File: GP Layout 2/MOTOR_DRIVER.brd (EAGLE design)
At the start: 91.4 x 97.5 mm, 82 parts, among them T1 2N2222, T2 2N2222, U7 ATMEGA328P_TQFP, Y1 16MHz

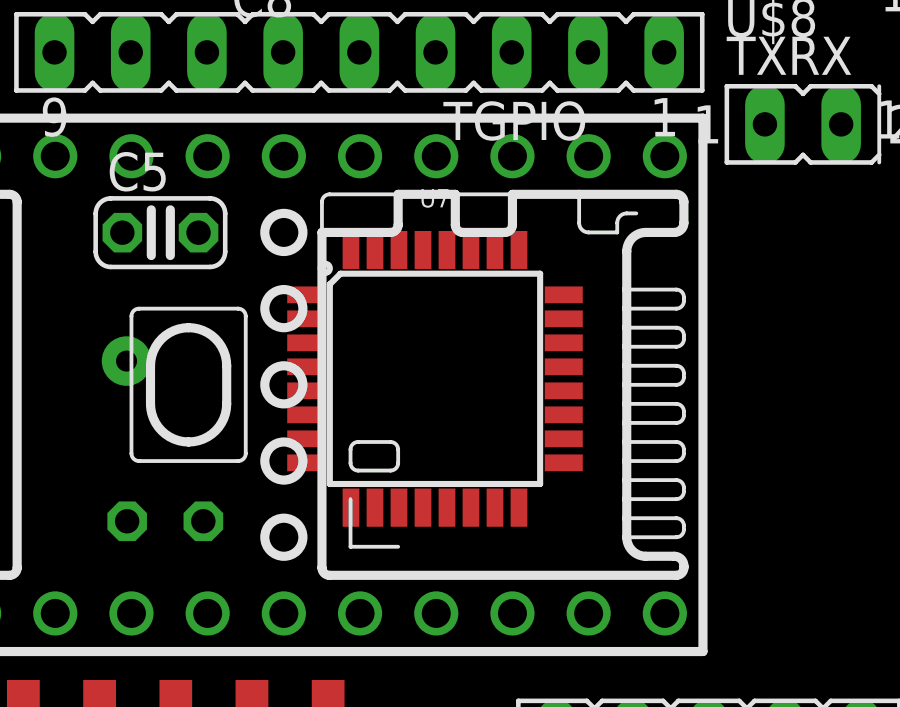
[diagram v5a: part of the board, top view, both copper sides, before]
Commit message: batt voltage connection fixed
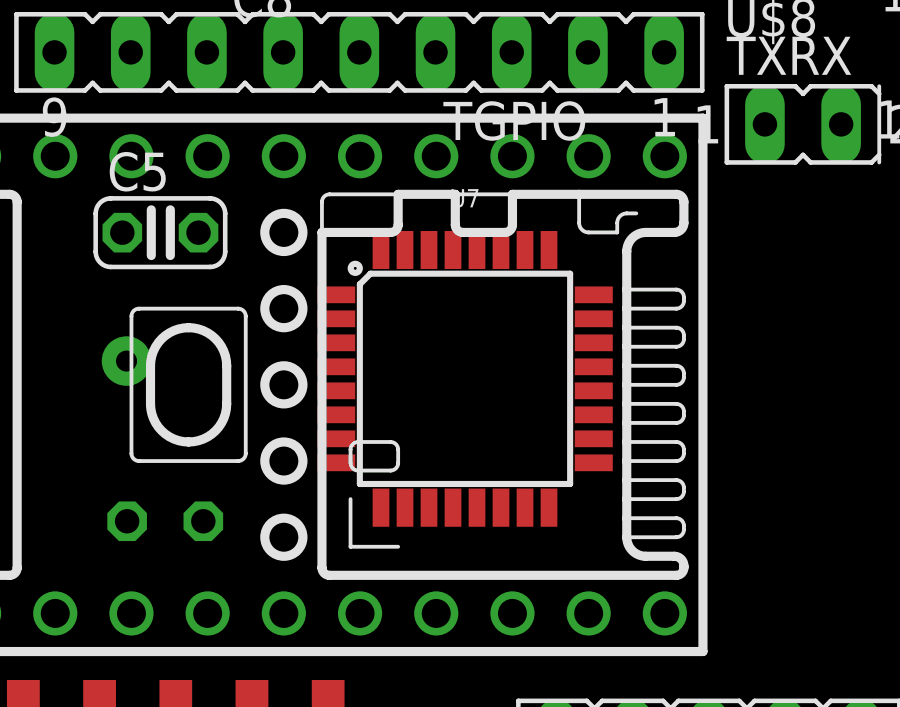
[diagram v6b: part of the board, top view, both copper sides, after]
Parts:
- moved U7 1.00 mm to (55.9, 21.5)
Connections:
- net 7_4V: now also R1.2
- net BATT_VOLTAGE: no longer R1.2
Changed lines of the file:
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@@
 <attribute name="VENDOR" value="Microchip" x="34.88" y="74.33" size="1.778" layer="28" rot="MR270" display="off"/>
 </element>
-<element name="U7" library="SparkFun-IC-Microcontroller" package="TQFP32-08" value="ATMEGA328P_TQFP" x="54.922" y="21.518">
-<attribute name="PROD_ID" value="IC-09069" x="54.922" y="21.518" size="1.778" layer="27" display="off"/>
+<element name="U7" library="SparkFun-IC-Microcontroller" package="TQFP32-08" value="ATMEGA328P_TQFP" x="55.922" y="21.518">
+<attribute name="PROD_ID" value="IC-09069" x="55.922" y="21.518" size="1.778" layer="27" display="off"/>
 </element>
 <element name="Y1" library="SparkFun-Clocks" package="HC49US" value="16MHz" x="42.1" y="22.11" rot="MR0">
@@
 <wire x1="74.626" y1="30.162" x2="74.826" y2="34.402" width="0" layer="19" extent="1-1"/>
 <wire x1="74.55" y1="41.066" x2="74.826" y2="34.402" width="0" layer="19" extent="1-1"/>
-<wire x1="59.2146" y1="21.918" x2="74.626" y2="30.162" width="0" layer="19" extent="1-1"/>
-<wire x1="50.6294" y1="21.118" x2="59.2146" y2="21.918" width="0" layer="19" extent="1-1"/>
-<wire x1="50.6294" y1="22.718" x2="50.6294" y2="21.118" width="0" layer="19" extent="1-1"/>
-<wire x1="47.04" y1="26.39" x2="50.6294" y2="22.718" width="0" layer="19" extent="1-1"/>
-<wire x1="47.2" y1="16.77" x2="50.6294" y2="21.118" width="0" layer="19" extent="1-1"/>
+<wire x1="60.2146" y1="21.918" x2="74.626" y2="30.162" width="0" layer="19" extent="1-1"/>
+<wire x1="51.6294" y1="21.118" x2="60.2146" y2="21.918" width="0" layer="19" extent="1-1"/>
+<wire x1="51.6294" y1="22.718" x2="51.6294" y2="21.118" width="0" layer="19" extent="1-1"/>
+<wire x1="47.04" y1="26.39" x2="51.6294" y2="22.718" width="0" layer="19" extent="1-1"/>
+<wire x1="47.2" y1="16.77" x2="51.6294" y2="21.118" width="0" layer="19" extent="1-1"/>
 <wire x1="46.28" y1="10.4758" x2="47.2" y2="16.77" width="0" layer="19" extent="1-1"/>
 <wire x1="43.74" y1="10.4758" x2="46.28" y2="10.4758" width="0" layer="19" extent="1-1"/>
@@
 <wire x1="24.414" y1="33.51" x2="33.02" y2="40.64" width="0" layer="19" extent="1-1"/>
 <wire x1="25.302" y1="22.49" x2="24.414" y2="33.51" width="0" layer="19" extent="1-1"/>
-<wire x1="69.13" y1="9.514" x2="59.2146" y2="21.918" width="0" layer="19" extent="1-1"/>
+<wire x1="69.13" y1="9.514" x2="60.2146" y2="21.918" width="0" layer="19" extent="1-1"/>
 <wire x1="75.142" y1="9.45" x2="69.13" y2="9.514" width="0" layer="19" extent="1-1"/>
 <wire x1="89" y1="10.54" x2="75.142" y2="9.45" width="0" layer="19" extent="1-1"/>
@@
 <contactref element="C6" pad="1"/>
 <contactref element="Y1" pad="1"/>
-<wire x1="44.64" y1="22.11" x2="50.6294" y2="19.518" width="0" layer="19" extent="1-1"/>
+<wire x1="44.64" y1="22.11" x2="51.6294" y2="19.518" width="0" layer="19" extent="1-1"/>
 <wire x1="44.66" y1="16.77" x2="44.64" y2="22.11" width="0" layer="19" extent="1-1"/>
 </signal>
@@
 <contactref element="U7" pad="8"/>
 <wire x1="39.56" y1="22.11" x2="44.5" y2="26.39" width="0" layer="19" extent="1-1"/>
-<wire x1="50.6294" y1="18.718" x2="39.56" y2="22.11" width="0" layer="19" extent="1-1"/>
+<wire x1="51.6294" y1="18.718" x2="39.56" y2="22.11" width="0" layer="19" extent="1-1"/>
 </signal>
 <signal name="SPI_MOSI">
@@
 <contactref element="U7" pad="15"/>
 <contactref element="PROGRAM" pad="4"/>
-<wire x1="37.184" y1="13.698" x2="56.922" y2="17.2254" width="0" layer="19" extent="1-1"/>
+<wire x1="37.184" y1="13.698" x2="57.922" y2="17.2254" width="0" layer="19" extent="1-1"/>
 <wire x1="85.54" y1="23.26" x2="37.184" y2="13.698" width="0" layer="19" extent="1-1"/>
 </signal>
@@
 <contactref element="U$1" pad="13/SCK"/>
 <contactref element="PROGRAM" pad="3"/>
-<wire x1="37.184" y1="28.938" x2="59.2146" y2="18.718" width="0" layer="19" extent="1-1"/>
+<wire x1="37.184" y1="28.938" x2="60.2146" y2="18.718" width="0" layer="19" extent="1-1"/>
 <wire x1="83" y1="23.26" x2="37.184" y2="28.938" width="0" layer="19" extent="1-1"/>
 </signal>
@@
 <contactref element="U$1" pad="11/MOSI"/>
 <contactref element="PROGRAM" pad="1"/>
-<wire x1="34.644" y1="13.698" x2="57.722" y2="17.2254" width="0" layer="19" extent="1-1"/>
+<wire x1="34.644" y1="13.698" x2="58.722" y2="17.2254" width="0" layer="19" extent="1-1"/>
 <wire x1="83" y1="25.8" x2="34.644" y2="13.698" width="0" layer="19" extent="1-1"/>
 </signal>
@@
 <contactref element="U7" pad="11"/>
 <contactref element="CAMERA" pad="5"/>
-<wire x1="53.722" y1="17.2254" x2="85.302" y2="9.45" width="0" layer="19" extent="1-1"/>
+<wire x1="54.722" y1="17.2254" x2="85.302" y2="9.45" width="0" layer="19" extent="1-1"/>
 </signal>
 <signal name="CAMERA_A0">
 <contactref element="U7" pad="23"/>
 <contactref element="CAMERA" pad="3"/>
-<wire x1="59.2146" y1="23.518" x2="80.222" y2="9.45" width="0" layer="19" extent="1-1"/>
+<wire x1="60.2146" y1="23.518" x2="80.222" y2="9.45" width="0" layer="19" extent="1-1"/>
 </signal>
 <signal name="SERVO">
@@
 <contactref element="U7" pad="14"/>
 <contactref element="U$1" pad="10/CS"/>
-<wire x1="32.104" y1="13.698" x2="56.122" y2="17.2254" width="0" layer="19" extent="1-1"/>
+<wire x1="32.104" y1="13.698" x2="57.122" y2="17.2254" width="0" layer="19" extent="1-1"/>
 </signal>
 <signal name="RX">
 <contactref element="U7" pad="30"/>
 <contactref element="TXRX" pad="1"/>
-<wire x1="65.92" y1="30" x2="53.722" y2="25.8106" width="0" layer="19" extent="1-1"/>
+<wire x1="65.92" y1="30" x2="54.722" y2="25.8106" width="0" layer="19" extent="1-1"/>
 </signal>
 <signal name="TX">
 <contactref element="U7" pad="31"/>
 <contactref element="TXRX" pad="2"/>
-<wire x1="68.46" y1="30" x2="52.922" y2="25.8106" width="0" layer="19" extent="1-1"/>
+<wire x1="68.46" y1="30" x2="53.922" y2="25.8106" width="0" layer="19" extent="1-1"/>
 </signal>
 <signal name="5V">
@@
 <contactref element="U7" pad="18"/>
 <contactref element="U7" pad="29"/>
-<wire x1="59.2146" y1="19.518" x2="51.36" y2="1.4842" width="0" layer="19" extent="1-1"/>
-<wire x1="54.522" y1="25.8106" x2="59.2146" y2="19.518" width="0" layer="19" extent="1-1"/>
-<wire x1="50.6294" y1="21.918" x2="54.522" y2="25.8106" width="0" layer="19" extent="1-1"/>
-<wire x1="50.6294" y1="20.318" x2="50.6294" y2="21.918" width="0" layer="19" extent="1-1"/>
-<wire x1="4.164" y1="28.938" x2="50.6294" y2="21.918" width="0" layer="19" extent="1-1"/>
+<wire x1="60.2146" y1="19.518" x2="51.36" y2="1.4842" width="0" layer="19" extent="1-1"/>
+<wire x1="55.522" y1="25.8106" x2="60.2146" y2="19.518" width="0" layer="19" extent="1-1"/>
+<wire x1="51.6294" y1="21.918" x2="55.522" y2="25.8106" width="0" layer="19" extent="1-1"/>
+<wire x1="51.6294" y1="20.318" x2="51.6294" y2="21.918" width="0" layer="19" extent="1-1"/>
+<wire x1="4.164" y1="28.938" x2="51.6294" y2="21.918" width="0" layer="19" extent="1-1"/>
 </signal>
 <signal name="GND_TOP">
@@
 <contactref element="VOLT_REG" pad="3"/>
 <contactref element="SV1" pad="7"/>
+<contactref element="R1" pad="2"/>
 <wire x1="25.4" y1="40.64" x2="48.766" y2="40.246" width="0" layer="19" extent="1-1"/>
+<wire x1="32.058" y1="22.49" x2="25.4" y2="40.64" width="0" layer="19" extent="1-1"/>
 </signal>
 <signal name="BATT_VOLTAGE">
@@
 <contactref element="FUSE" pad="C"/>
 <contactref element="FUSE" pad="A"/>
-<contactref element="R1" pad="2"/>
-<wire x1="14.888" y1="75.846" x2="32.058" y2="22.49" width="0" layer="19" extent="1-1"/>
+<wire x1="14.888" y1="75.846" x2="6.27" y2="83.01" width="0" layer="19" extent="1-1"/>
 <wire x1="14.888" y1="69.786" x2="14.888" y2="75.846" width="0" layer="19" extent="1-1"/>
-<wire x1="6.27" y1="83.01" x2="14.888" y2="69.786" width="0" layer="19" extent="1-1"/>
 </signal>
 <signal name="N$21">
@@
 <contactref element="U7" pad="32"/>
 <contactref element="HALL1" pad="3"/>
-<wire x1="52.122" y1="25.8106" x2="77.366" y2="34.402" width="0" layer="19" extent="1-1"/>
+<wire x1="53.122" y1="25.8106" x2="77.366" y2="34.402" width="0" layer="19" extent="1-1"/>
 </signal>
 <signal name="CAMERA_CL">
 <contactref element="CAMERA" pad="4"/>
 <contactref element="U7" pad="12"/>
-<wire x1="54.522" y1="17.2254" x2="82.762" y2="9.45" width="0" layer="19" extent="1-1"/>
+<wire x1="55.522" y1="17.2254" x2="82.762" y2="9.45" width="0" layer="19" extent="1-1"/>
 </signal>
 <signal name="CAMERA_SI_B">
@@
 <contactref element="HALL2" pad="3"/>
 <contactref element="U7" pad="1"/>
-<wire x1="50.6294" y1="24.318" x2="77.166" y2="30.162" width="0" layer="19" extent="1-1"/>
+<wire x1="51.6294" y1="24.318" x2="77.166" y2="30.162" width="0" layer="19" extent="1-1"/>
 </signal>
 <signal name="HALL1_B">

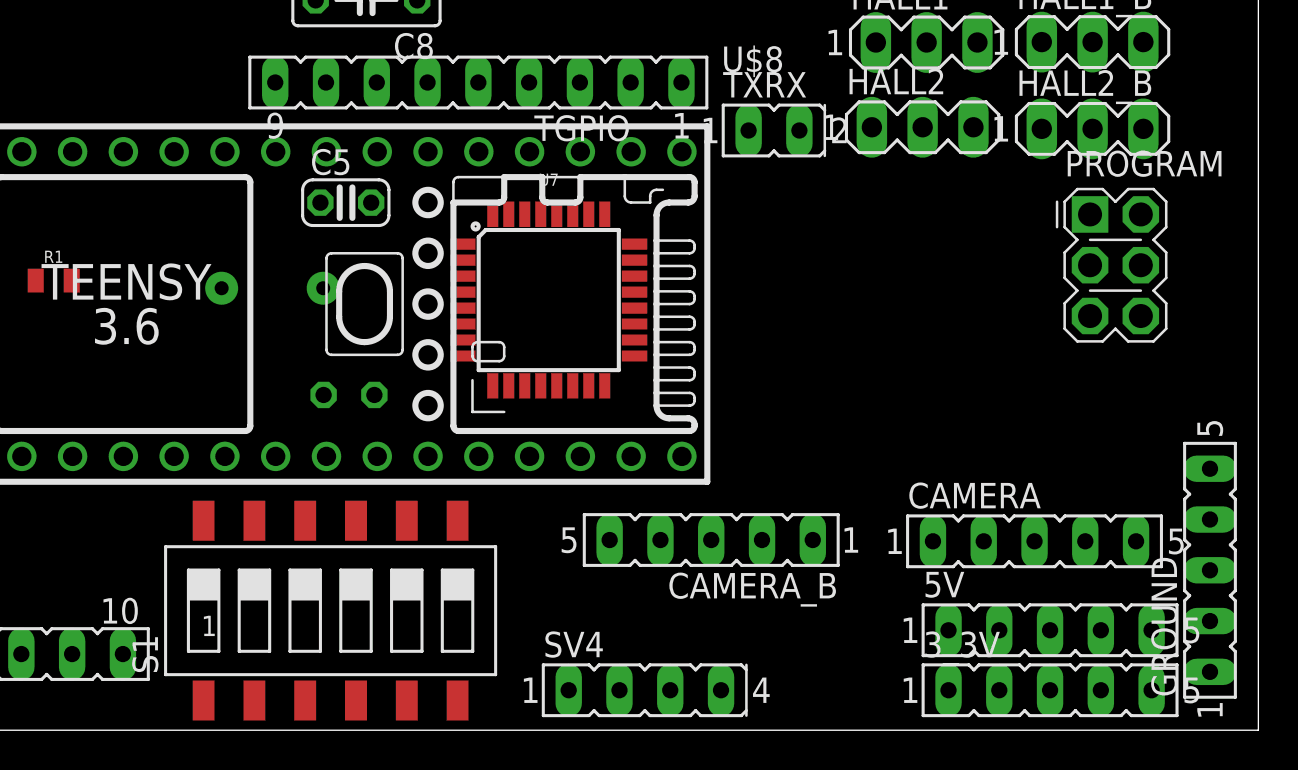
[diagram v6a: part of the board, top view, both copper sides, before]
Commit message: moved dip switch
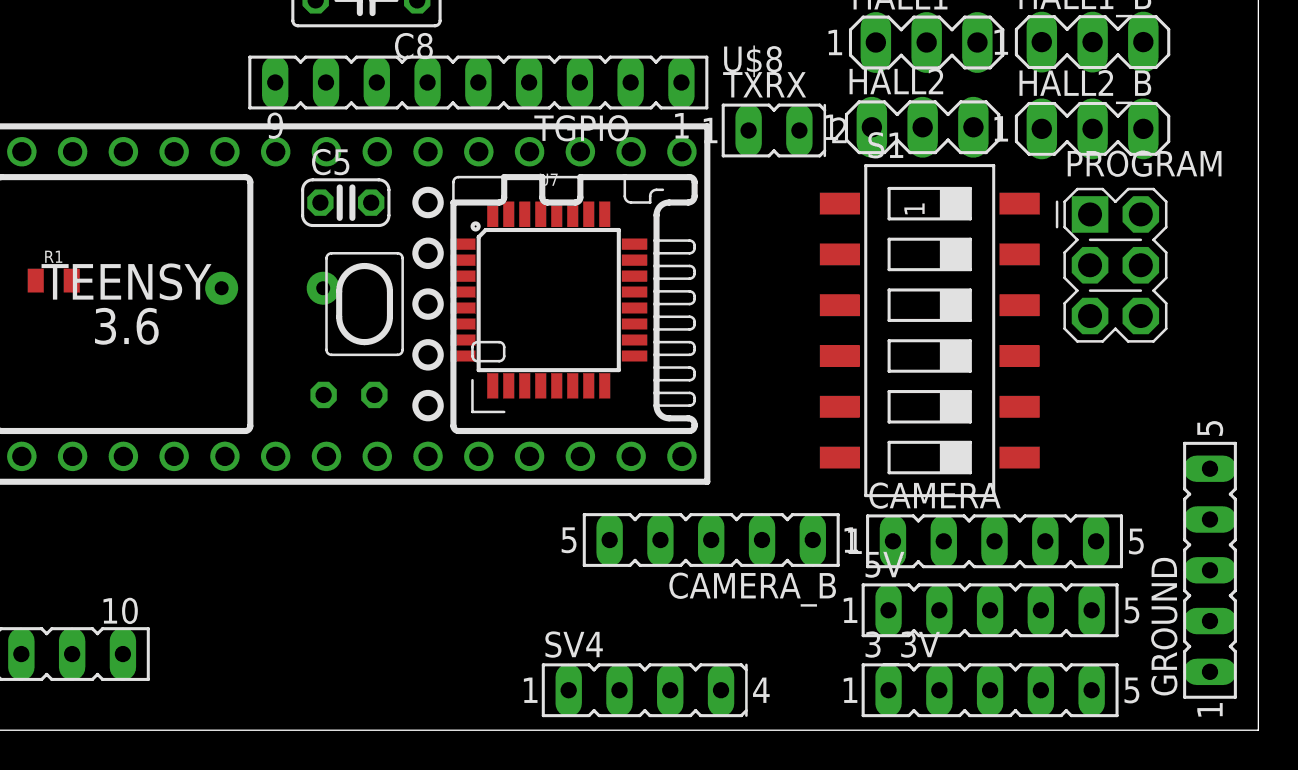
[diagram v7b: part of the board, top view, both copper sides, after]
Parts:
- moved S1 33.1 mm to (75.0, 20.0), turned to 270 degrees
- moved 5V 3.16 mm to (78.0, 6.00)
- moved 3_3V 3.00 mm to (78.0, 2.00)
- moved CAMERA 2.00 mm to (78.2, 9.45)
